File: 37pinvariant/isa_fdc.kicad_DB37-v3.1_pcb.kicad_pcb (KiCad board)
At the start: 2 copper layers, 106.5 x 88.1 mm, 29 parts, among them P1 FLOPPY, P2 DB37 Female (External Floppy), P3 FLOPPY, SW1 FDC_CONFIG, SW2 ROM_CONFIG, U1 82077AA, U2 74LS125, U4 28C64, U5 74LS688, U6 74ALS138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

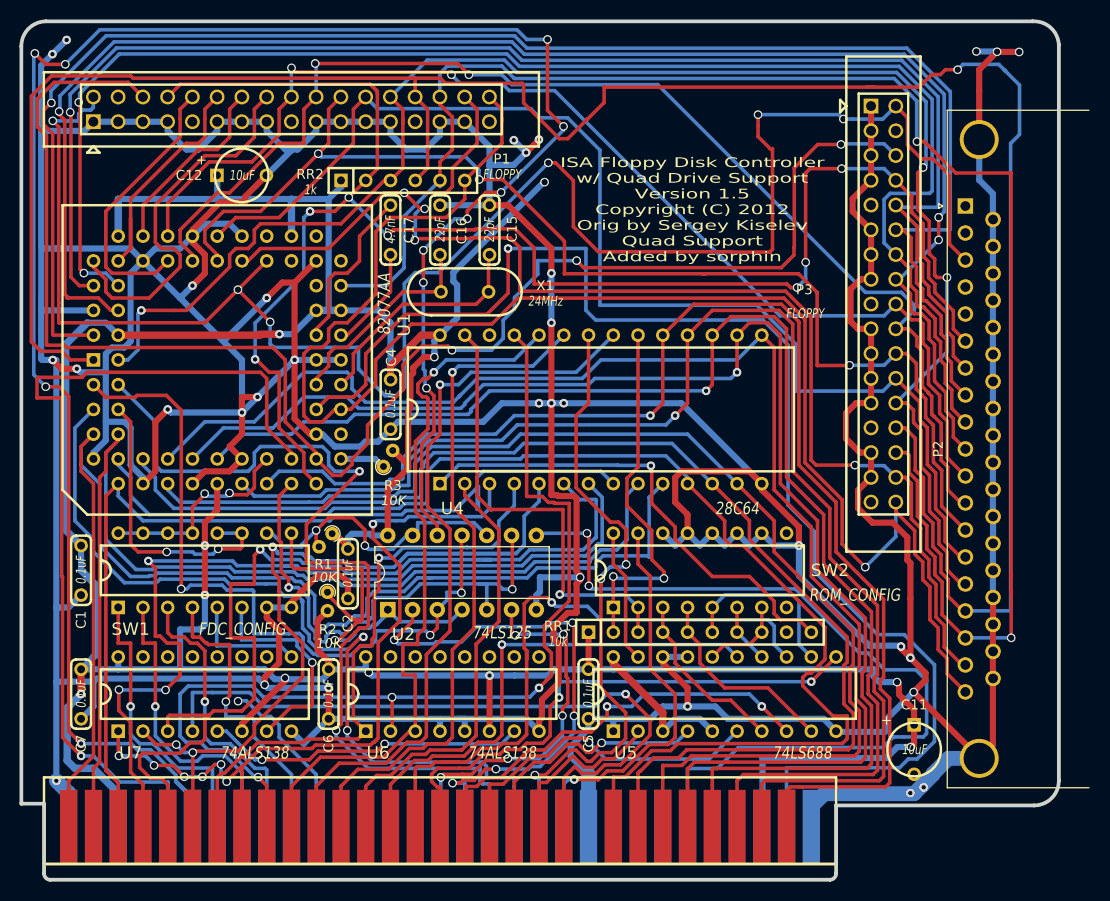
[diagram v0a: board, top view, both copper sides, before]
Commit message: adjust DC-37 fitment and lower ISA contact fingers
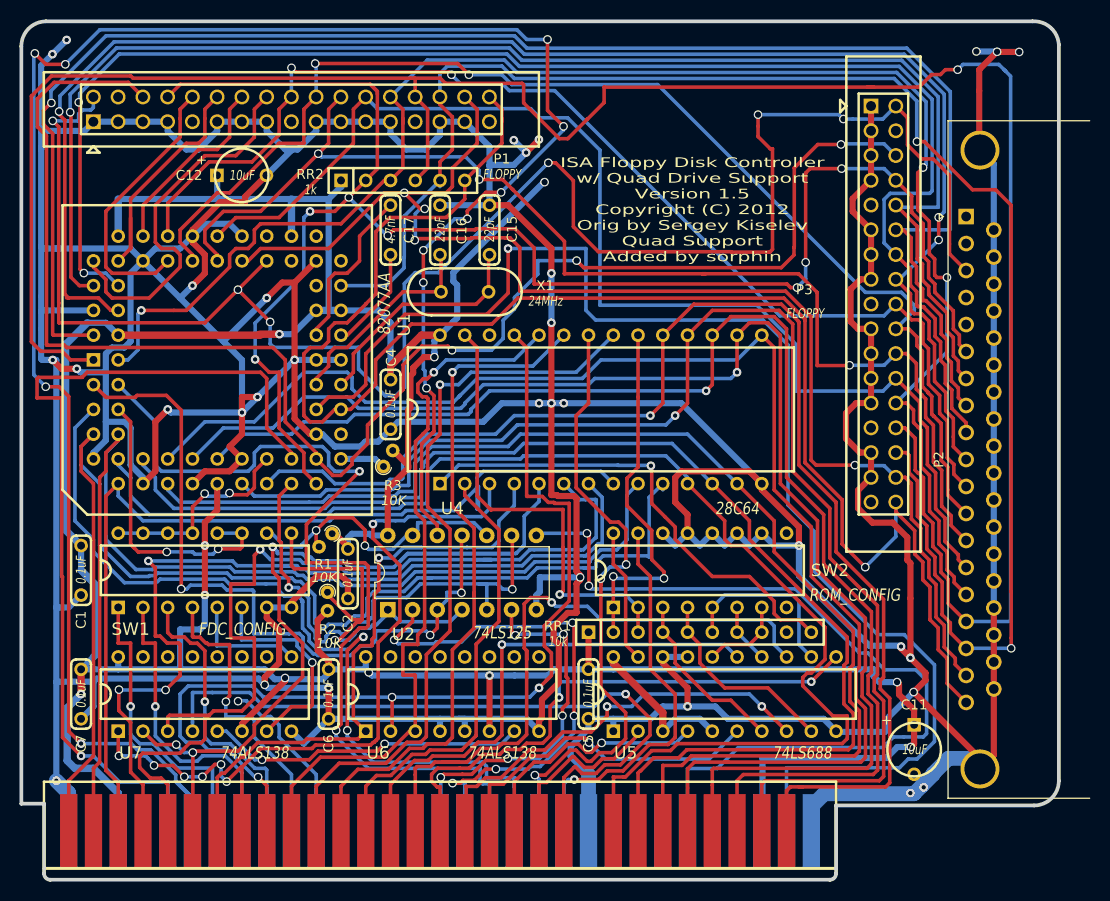
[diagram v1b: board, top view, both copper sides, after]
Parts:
- moved P2 1.08 mm to (196.2, 66.6)
- moved BUS1 0.44 mm to (142.2, 129.6)
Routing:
- net GND: track 866.4 -> 869.6 mm
- net /DIR: track 119.4 -> 120.5 mm
- net /DSKCG: track 164.8 -> 165.9 mm
- net /DS3: track 167.3 -> 168.4 mm
- net /ME3: track 164.3 -> 165.5 mm
- net /ME2: track 150.1 -> 151.2 mm
- net /INDEX: track 167.8 -> 168.9 mm
- net /DS2: track 155.2 -> 156.3 mm
- net /DENSL: track 185.0 -> 186.1 mm
- net /WDATA: track 123.2 -> 124.3 mm
- net /HDSEL: track 136.2 -> 137.1 mm
- net /D7: track 136.7 -> 135.8 mm
- net /A17: track 34.7 -> 33.8 mm
- net /TRK00: track 166.0 -> 166.9 mm
- net /STEP: track 125.9 -> 126.8 mm
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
